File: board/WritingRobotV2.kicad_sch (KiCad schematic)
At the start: 7 parts, among them J1 Conn_01x02_Socket, J2 Conn_01x04_Pin, J3 Conn_01x04_Pin, J4 Conn_01x06_Socket

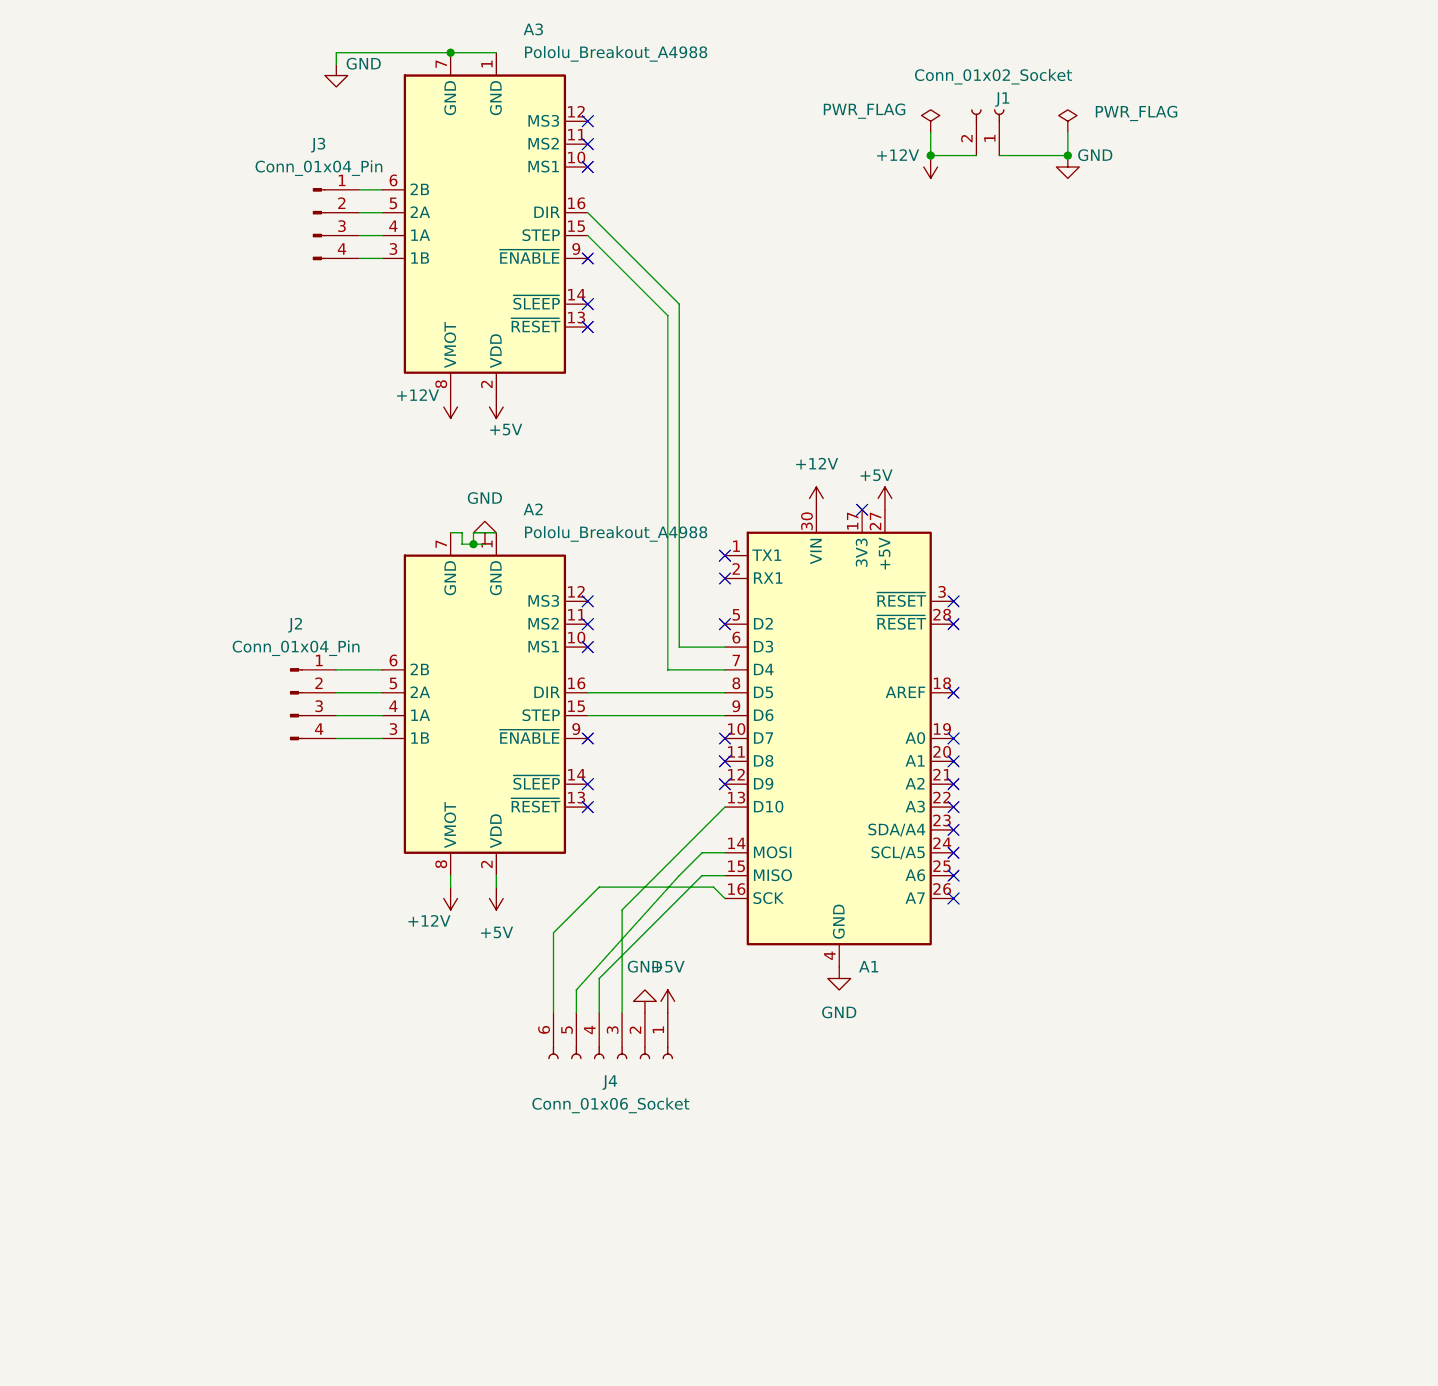
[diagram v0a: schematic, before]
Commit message: Changed electrical layout Added 3d components to PCB Created photos for DOCU Modified Readme file
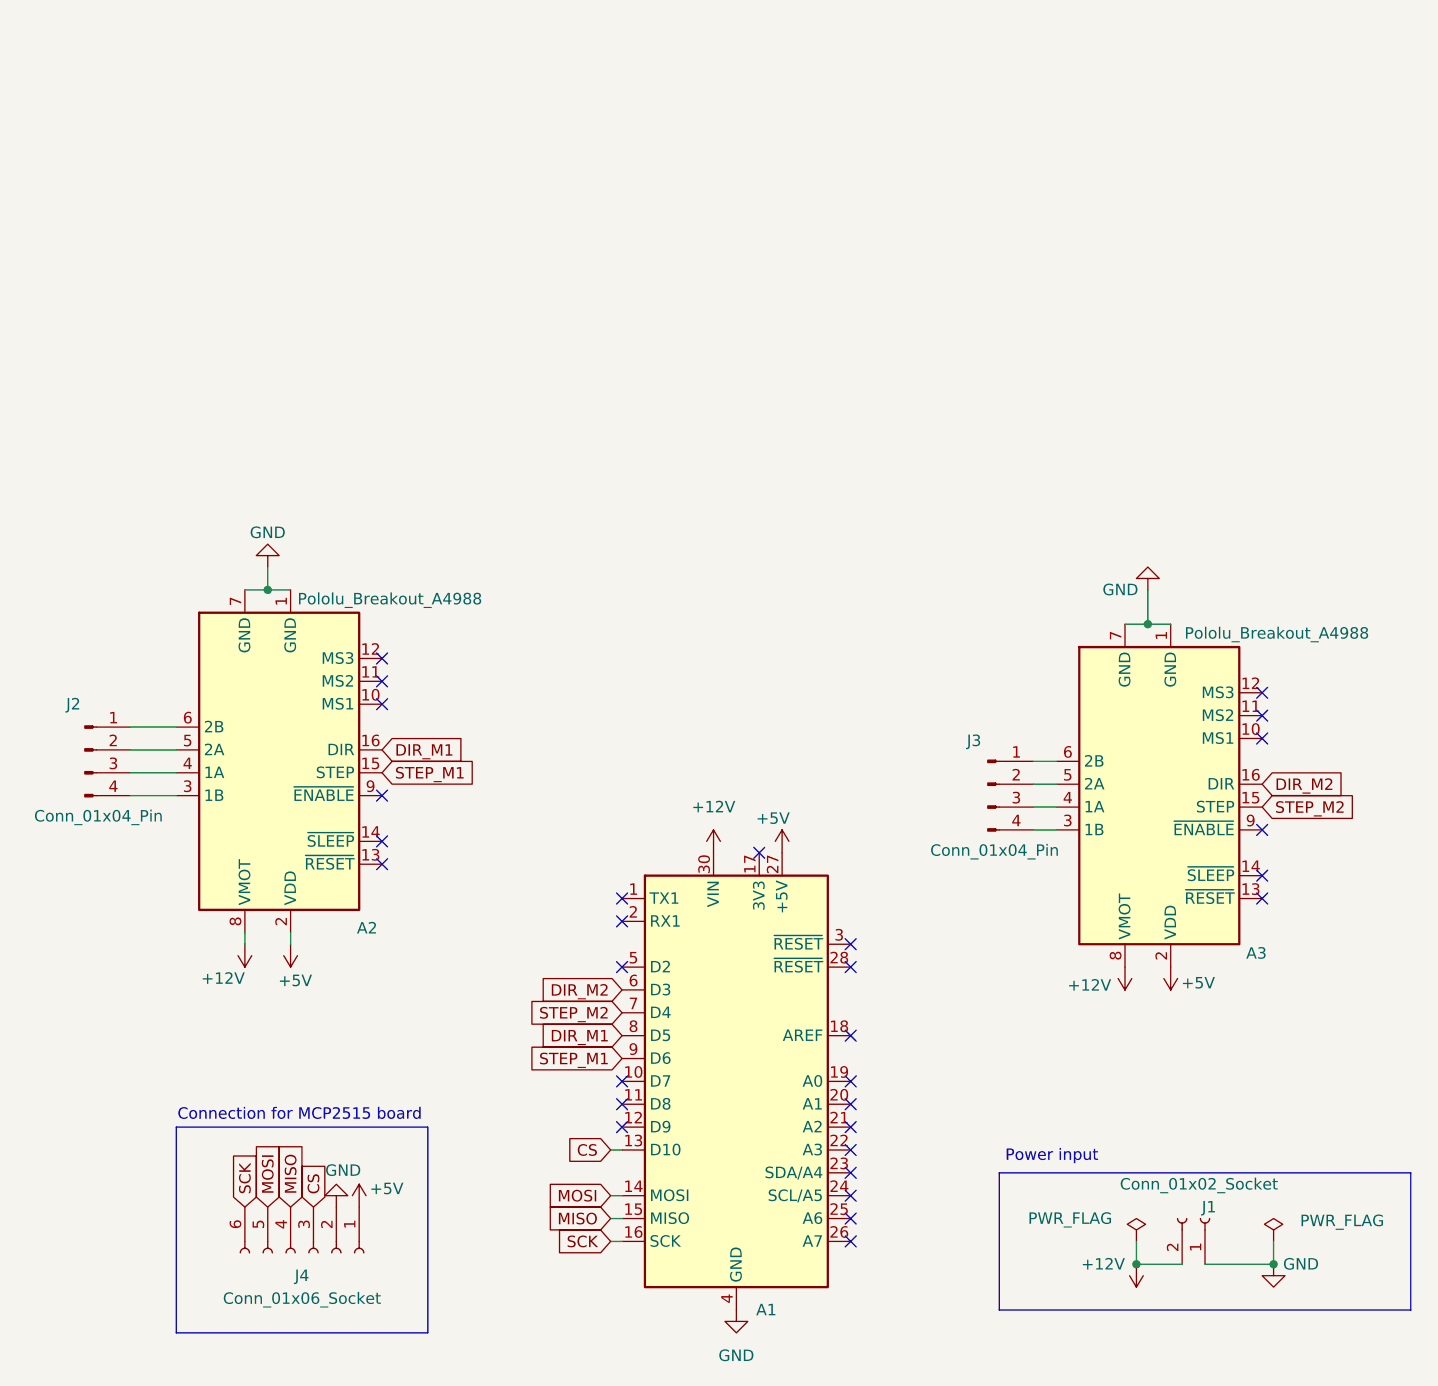
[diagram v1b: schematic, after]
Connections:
- net STEP_M2: now reaches A1.7 (D4), A3.15 (STEP)
- net DIR_M2: now reaches A1.6 (D3), A3.16 (DIR)
- net STEP_M1: now reaches A1.9 (D6), A2.15 (STEP)
- net DIR_M1: now reaches A1.8 (D5), A2.16 (DIR)
- net CS: now reaches A1.13 (D10), J4.3 (Pin_3)
- net MISO: now reaches A1.15 (MISO), J4.4 (Pin_4)
- net MOSI: now reaches A1.14 (MOSI), J4.5 (Pin_5)
- net SCK: now reaches A1.16 (SCK), J4.6 (Pin_6)
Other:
- note added: "Connection for MCP2515 board"
- note added: "Power input"
- moved on the sheet: A1, A2, A3, J1, J2, J3, J4

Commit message: Board updated
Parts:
- added C1: C_Polarized, Capacitor_THT:CP_Radial_D5.0mm_P2.50mm, symbol Device:C_Polarized
- added C2: C, Capacitor_THT:C_Rect_L4.0mm_W2.5mm_P2.50mm, symbol Device:C
- added H1, H3, H4: MountingHole, MountingHole:MountingHole_4.3mm_M4, symbol Mechanical:MountingHole
- added R1: R, Resistor_THT:R_Axial_DIN0411_L9.9mm_D3.6mm_P7.62mm_Vertical, symbol Device:R
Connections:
- net +12V: now also C1.1, C2.1, R1.1; no longer J1.2 (Pin_2)
- net +5V: now also A2.10 (MS1), A2.11 (MS2), A2.12 (MS3), A3.10 (MS1), A3.11 (MS2), A3.12 (MS3)
- net GND: now also C1.2, C2.2
- net at A3.13 (~{RESET}): now also A3.14 (~{SLEEP})
- net at A2.13 (~{RESET}): now also A2.14 (~{SLEEP})
- new net: J1.2 (Pin_2), R1.2
- no-connect marks 30 -> 20
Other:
- moved on the sheet: J1

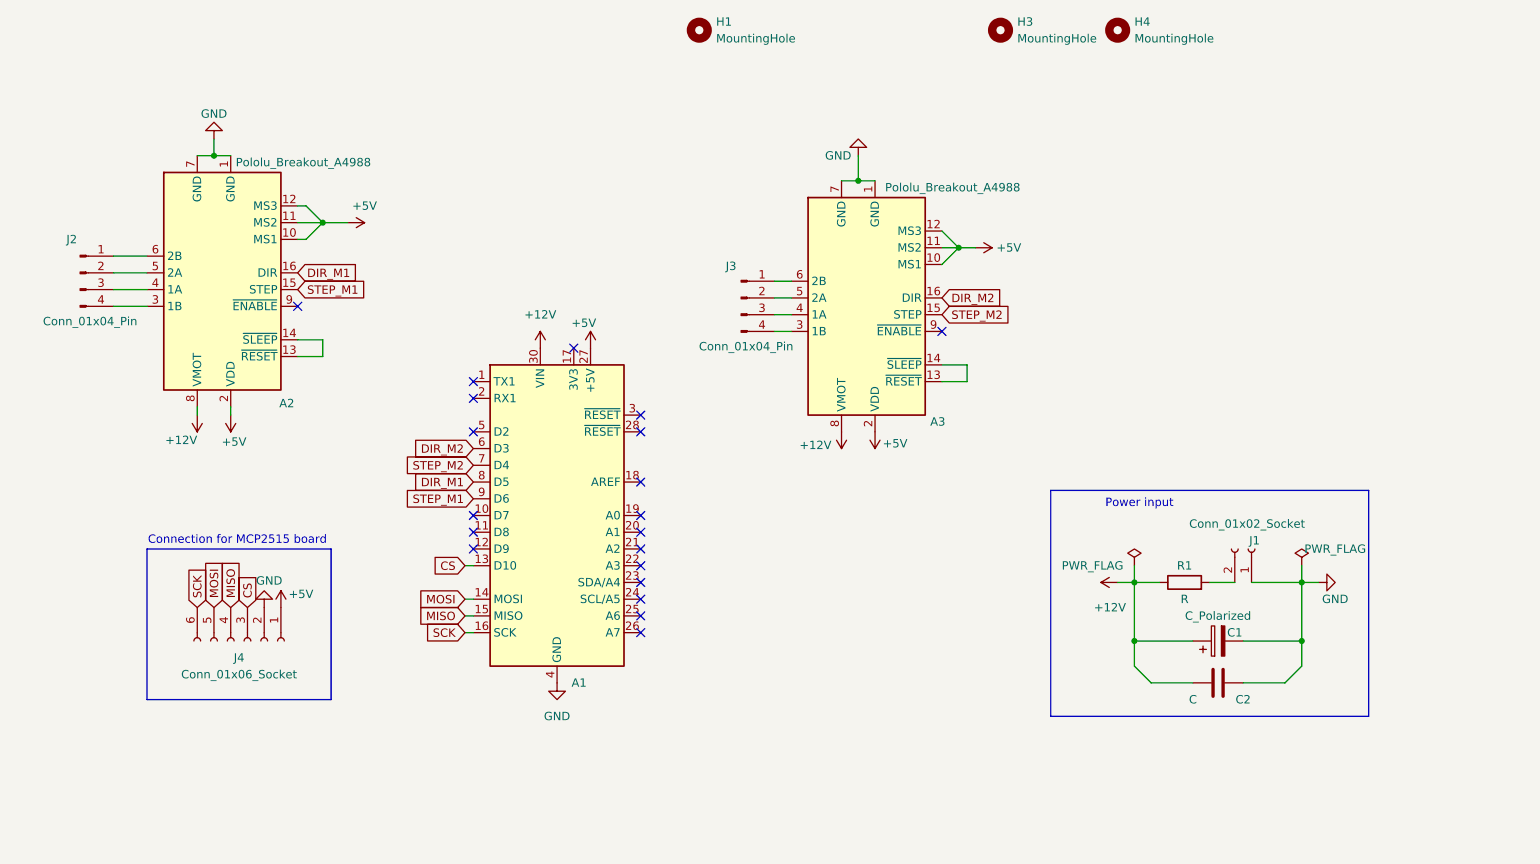
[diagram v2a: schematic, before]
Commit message: Board to stm32
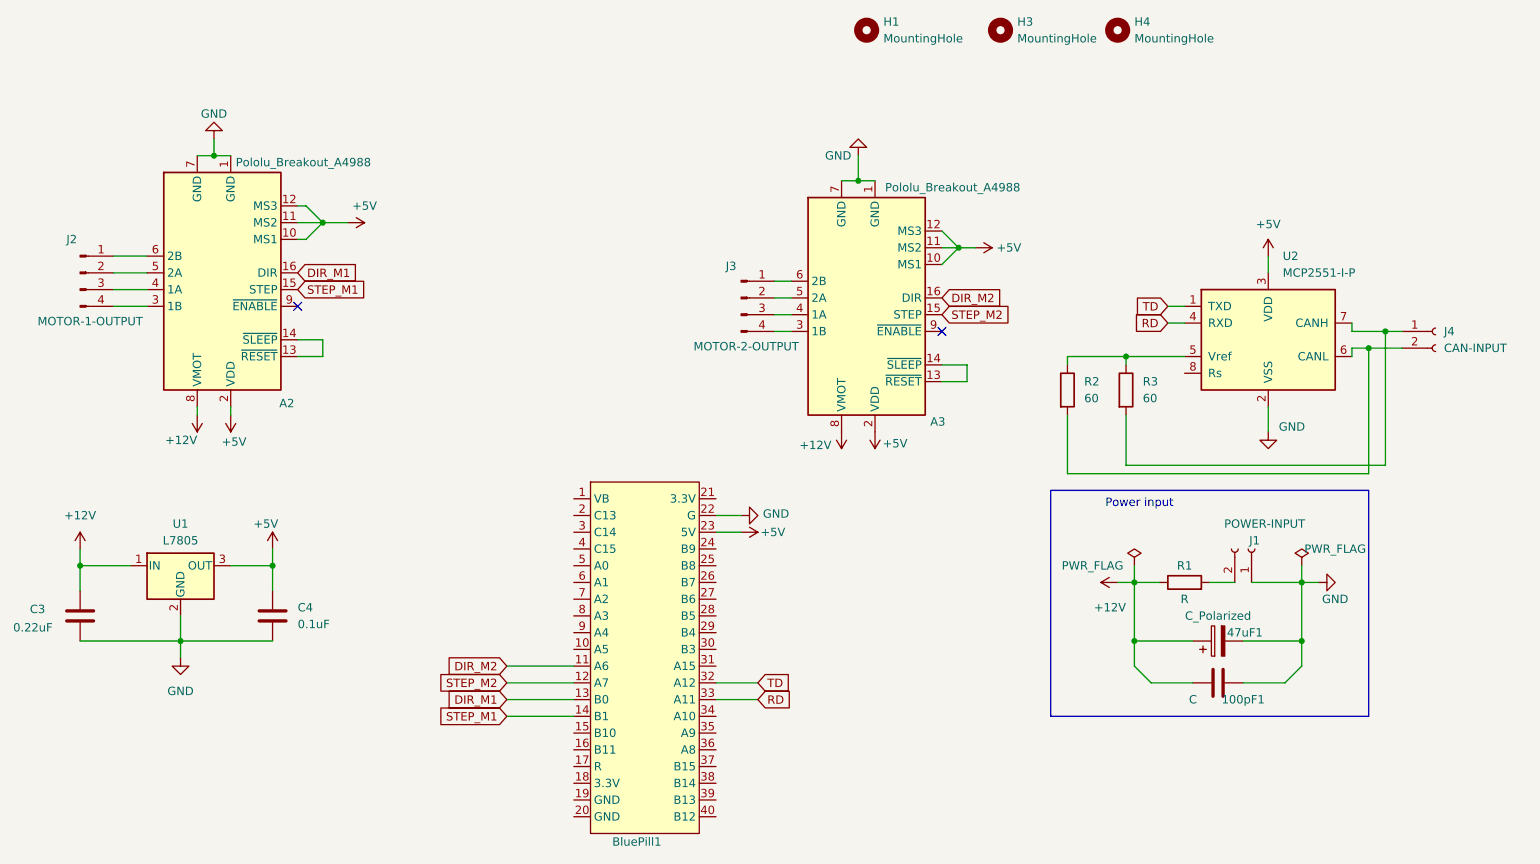
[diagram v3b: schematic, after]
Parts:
- removed A1: Arduino_Nano_Every, Module:Arduino_Nano, symbol MCU_Module:Arduino_Nano_Every
- removed J4: Conn_01x06_Socket, Connector_PinSocket_2.54mm:PinSocket_1x06_P2.54mm_Vertical, symbol Connector:Conn_01x06_Socket
- added BluePill1: ~, STM32_Bluepill:BluePill, symbol STM32BLUPILL:BluePIll
- added C3: 0.22uF, Capacitor_THT:C_Radial_D10.0mm_H16.0mm_P5.00mm, symbol Device:C
- added C4: 0.1uF, Capacitor_THT:C_Rect_L4.0mm_W2.5mm_P2.50mm, symbol Device:C
- added J4: CAN-INPUT, Connector_PinSocket_2.54mm:PinSocket_1x02_P2.54mm_Vertical, symbol Connector:Conn_01x02_Socket
- added R2, R3: 60, Resistor_THT:R_Axial_DIN0204_L3.6mm_D1.6mm_P7.62mm_Horizontal, symbol Device:R
- added U1: L7805, Connector_PinHeader_2.54mm:PinHeader_1x03_P2.54mm_Vertical, symbol Regulator_Linear:L7805
- added U2: MCP2551-I-P, Package_DIP:DIP-8_W7.62mm, symbol Interface_CAN_LIN:MCP2551-I-P
- J1: value Conn_01x02_Socket -> POWER-INPUT
- J2: value Conn_01x04_Pin -> MOTOR-1-OUTPUT
- J3: value Conn_01x04_Pin -> MOTOR-2-OUTPUT
- R1: footprint Resistor_THT:R_Axial_DIN0411_L9.9mm_D3.6mm_P7.62mm_Vertical -> Resistor_THT:R_Axial_DIN0204_L3.6mm_D1.6mm_P7.62mm_Horizontal
- renumbered C2 to 100pF1, C1 to 47uF1
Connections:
- net +12V: now also C3.1, U1.1 (IN)
- net +5V: now also BluePill1.23 (5V), C4.1, U1.3 (OUT), U2.3 (VDD)
- net DIR_M1: now also BluePill1.13 (B0)
- net DIR_M2: now also BluePill1.11 (A6)
- net GND: now also BluePill1.22 (G), C3.2, C4.2, U1.2 (GND), U2.2 (VSS)
- net STEP_M1: now also BluePill1.14 (B1)
- net STEP_M2: now also BluePill1.12 (A7)
- new net: J4.1 (Pin_1), R3.2, U2.7 (CANH)
- new net: J4.2 (Pin_2), R2.2, U2.6 (CANL)
- new net: R2.1, R3.1, U2.5 (Vref)
- new net RD: BluePill1.33 (A11), U2.4 (RXD)
- new net TD: BluePill1.32 (A12), U2.1 (TXD)
- no-connect marks 20 -> 2
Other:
- note removed: "Connection for MCP2515 board"
- moved on the sheet: H1
